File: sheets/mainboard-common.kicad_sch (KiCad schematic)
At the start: 46 parts, among them J1 Conn_01x04, J2 USB4105, J3 Conn_01x04, J4 Conn_01x16_Socket, J5 Conn_01x16_Socket, J6 Conn_01x16_Socket, J7 Conn_01x16_Socket, U2 AP22916, U3 AP22916

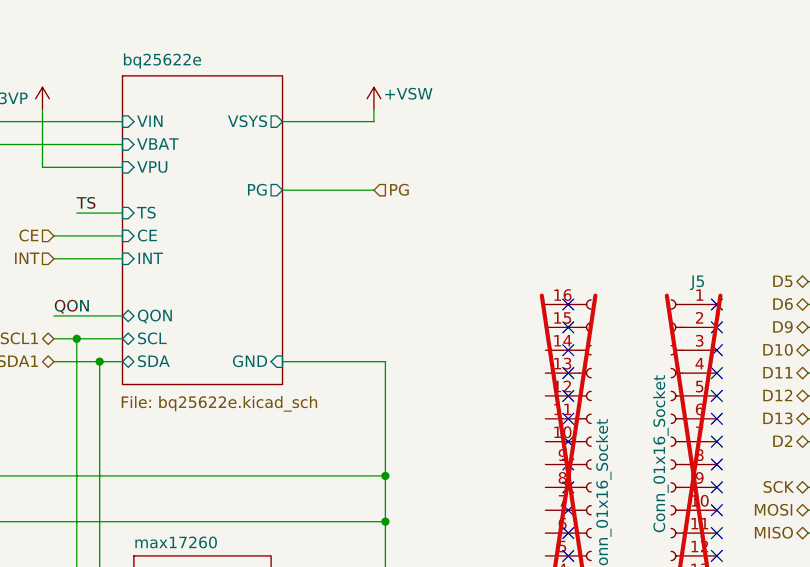
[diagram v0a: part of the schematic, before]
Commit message: Bring out ILIM
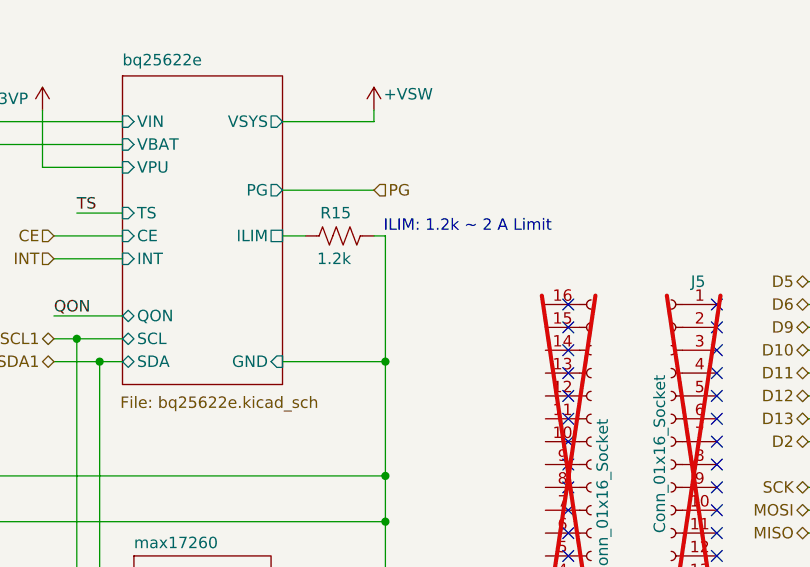
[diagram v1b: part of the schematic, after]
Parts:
- added R15: 1.2k, Resistor_SMD:R_0402_1005Metric, symbol Device:R_US
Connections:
- net GND: now also R15.2
- new net bq25622e/ILIM: R15.1
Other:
- sheet bq25622e ports: added ILIM; removed none
- note added: "ILIM: 1.2k ~ 2 A Limit"
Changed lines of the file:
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@@
 	)
 	(junction
+		(at 157.48 95.25)
+		(diameter 0)
+		(color 0 0 0 0)
+	)
+	(junction
 		(at 55.88 26.67)
 		(diameter 0)
@@
 	(wire
 		(pts
+			(xy 146.05 81.28) (xy 148.59 81.28)
+		)
+		(stroke
+			(width 0)
+			(type default)
+		)
+	)
+	(wire
+		(pts
 			(xy 146.05 30.48) (xy 146.05 33.02)
 		)
@@
 	(wire
 		(pts
+			(xy 157.48 81.28) (xy 157.48 95.25)
+		)
+		(stroke
+			(width 0)
+			(type default)
+		)
+	)
+	(wire
+		(pts
 			(xy 144.78 130.81) (xy 148.59 130.81)
 		)
@@
 	(wire
 		(pts
+			(xy 156.21 81.28) (xy 157.48 81.28)
+		)
+		(stroke
+			(width 0)
+			(type default)
+		)
+	)
+	(wire
+		(pts
 			(xy 247.65 35.56) (xy 245.11 35.56)
 		)
@@
 		)
 	)
+	(text "ILIM: 1.2k ~ 2 A Limit"
+		(exclude_from_sim no)
+		(at 166.624 80.264 0)
+		(effects
+			(font
+				(size 1.27 1.27)
+			)
+		)
+	)
 	(label "QON"
 		(at 242.57 96.52 180)
@@
 	)
 	(symbol
+		(lib_id "Device:R_US")
+		(at 152.4 81.28 90)
+		(unit 1)
+		(exclude_from_sim no)
+		(in_bom yes)
+		(on_board yes)
+		(dnp no)
+		(property "Reference" "R15"
+			(at 153.67 78.74 90)
+			(effects
+				(font
+					(size 1.27 1.27)
+				)
+				(justify left)
+			)
+		)
+		(property "Value" "1.2k"
+			(at 153.67 83.82 90)
+			(effects
+				(font
+					(size 1.27 1.27)
+				)
+				(justify left)
+			)
+		)
+		(property "Footprint" "Resistor_SMD:R_0402_1005Metric"
+			(at 152.654 80.264 90)
+			(effects
+				(font
+					(size 1.27 1.27)
+				)
+				(hide yes)
+			)
+		)
+		(property "Datasheet" ""
+			(at 152.4 81.28 0)
+			(effects
+				(font
+					(size 1.27 1.27)
+				)
+				(hide yes)
+			)
+		)
+		(property "Description" ""
+			(at 152.4 81.28 0)
+			(effects
+				(font
+					(size 1.27 1.27)
+				)
+				(hide yes)
+			)
+		)
+		(property "MPN" ""
+			(at 152.4 81.28 0)
+			(effects
+				(font
+					(size 1.27 1.27)
+				)
+				(hide yes)
+			)
+		)
+		(pin "1"
+		)
+		(pin "2"
+		)
+		(instances
+			(project "esp32s3-powerfeather"
+				(path "/5be6a852-fa78-49fa-bb8c-8d5ad39f4b26/a940761a-0d45-4491-ba89-ec093a8f239f"
+					(reference "R15")
+					(unit 1)
+				)
+			)
+		)
+	)
+	(symbol
 		(lib_id "Connector:TestPoint")
 		(at 71.12 171.45 270)
@@
 			)
 		)
+		(pin "ILIM" passive
+			(at 146.05 81.28 0)
+			(effects
+				(font
+					(size 1.27 1.27)
+				)
+				(justify right)
+			)
+		)

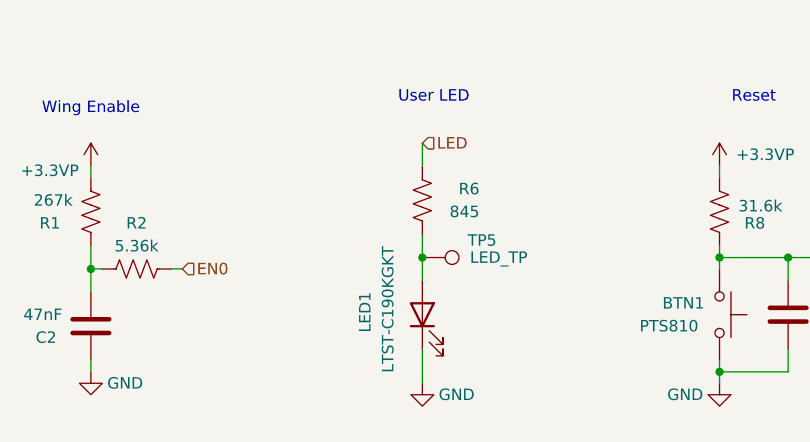
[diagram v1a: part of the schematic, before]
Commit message: Use same 1.2k for LED
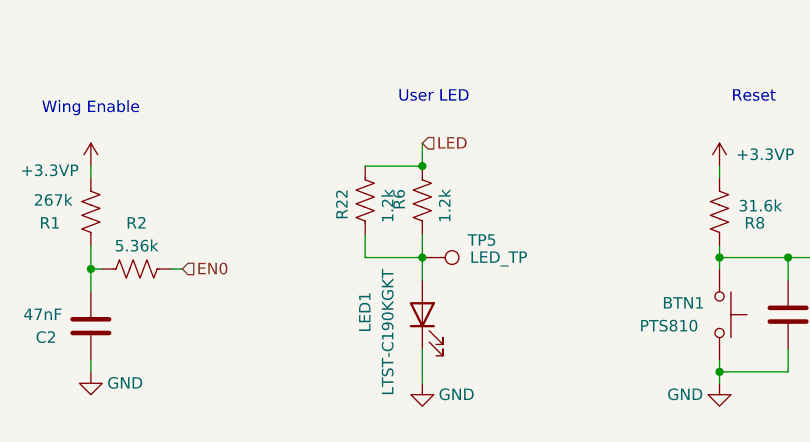
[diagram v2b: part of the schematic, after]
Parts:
- added R22: 1.2k, Resistor_SMD:R_0402_1005Metric, symbol Device:R_US
- R6: value 845 -> 1.2k; MPN 603-AC0402FR-07845RL -> (none)
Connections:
- net LED: now also R22.2
- net at LED1.2 (A), R6.1, TP5.1: now also R22.1
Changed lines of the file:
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@@
 	)
 	(junction
+		(at 71.12 161.29)
+		(diameter 0)
+		(color 0 0 0 0)
+	)
+	(junction
 		(at 143.51 171.45)
 		(diameter 0)
@@
 	(wire
 		(pts
+			(xy 64.77 161.29) (xy 71.12 161.29)
+		)
+		(stroke
+			(width 0)
+			(type default)
+		)
+	)
+	(wire
+		(pts
 			(xy 204.47 101.6) (xy 210.82 101.6)
 		)
@@
 	(wire
 		(pts
+			(xy 64.77 171.45) (xy 71.12 171.45)
+		)
+		(stroke
+			(width 0)
+			(type default)
+		)
+	)
+	(wire
+		(pts
 			(xy 33.02 102.87) (xy 33.02 107.95)
 		)
@@
 	(wire
 		(pts
+			(xy 64.77 168.91) (xy 64.77 171.45)
+		)
+		(stroke
+			(width 0)
+			(type default)
+		)
+	)
+	(wire
+		(pts
 			(xy 220.98 74.93) (xy 220.98 76.2)
 		)
@@
 		)
 		(property "Value" "LTST-C190KGKT"
-			(at 67.31 170.18 0)
+			(at 67.31 172.72 0)
 			(effects
 				(font
@@
 	(symbol
 		(lib_id "Device:R_US")
+		(at 71.12 165.1 180)
+		(unit 1)
+		(exclude_from_sim no)
+		(in_bom yes)
+		(on_board yes)
+		(dnp no)
+		(property "Reference" "R6"
+			(at 68.58 163.83 90)
+			(effects
+				(font
+					(size 1.27 1.27)
+				)
+				(justify left)
+			)
+		)
+		(property "Value" "1.2k"
+			(at 73.66 163.83 90)
+			(effects
+				(font
+					(size 1.27 1.27)
+				)
+				(justify left)
+			)
+		)
+		(property "Footprint" "Resistor_SMD:R_0402_1005Metric"
+			(at 70.104 164.846 90)
+			(effects
+				(font
+					(size 1.27 1.27)
+				)
+				(hide yes)
+			)
+		)
+		(property "Datasheet" ""
+			(at 71.12 165.1 0)
+			(effects
+				(font
+					(size 1.27 1.27)
+				)
+				(hide yes)
+			)
+		)
+		(property "Description" ""
+			(at 71.12 165.1 0)
+			(effects
+				(font
+					(size 1.27 1.27)
+				)
+				(hide yes)
+			)
+		)
+		(property "MPN" ""
+			(at 71.12 165.1 0)
+			(effects
+				(font
+					(size 1.27 1.27)
+				)
+				(hide yes)
+			)
+		)
+		(pin "1"
+		)
+		(pin "2"
+		)
+		(instances
+			(project "esp32s3-powerfeather"
+				(path "/5be6a852-fa78-49fa-bb8c-8d5ad39f4b26/a940761a-0d45-4491-ba89-ec093a8f239f"
+					(reference "R6")
+					(unit 1)
+				)
+			)
+		)
+	)
+	(symbol
+		(lib_id "Device:R_US")
 		(at 69.85 128.27 0)
 		(mirror y)
@@
 	(symbol
 		(lib_id "Device:R_US")
+		(at 64.77 165.1 180)
+		(unit 1)
+		(exclude_from_sim no)
+		(in_bom yes)
+		(on_board yes)
+		(dnp no)
+		(property "Reference" "R22"
+			(at 62.23 163.83 90)
+			(effects
+				(font
+					(size 1.27 1.27)
+				)
+				(justify left)
+			)
+		)
+		(property "Value" "1.2k"
+			(at 67.31 163.83 90)
+			(effects
+				(font
+					(size 1.27 1.27)
+				)
+				(justify left)
+			)
+		)
+		(property "Footprint" "Resistor_SMD:R_0402_1005Metric"
+			(at 63.754 164.846 90)
+			(effects
+				(font
+					(size 1.27 1.27)
+				)
+				(hide yes)
+			)
+		)
+		(property "Datasheet" ""
+			(at 64.77 165.1 0)
+			(effects
+				(font
+					(size 1.27 1.27)
+				)
+				(hide yes)
+			)
+		)
+		(property "Description" ""
+			(at 64.77 165.1 0)
+			(effects
+				(font
+					(size 1.27 1.27)
+				)
+				(hide yes)
+			)
+		)
+		(property "MPN" ""
+			(at 64.77 165.1 0)
+			(effects
+				(font
+					(size 1.27 1.27)
+				)
+				(hide yes)
+			)
+		)
+		(pin "1"
+		)
+		(pin "2"
+		)
+		(instances
+			(project "esp32s3-powerfeather"
+				(path "/5be6a852-fa78-49fa-bb8c-8d5ad39f4b26/a940761a-0d45-4491-ba89-ec093a8f239f"
+					(reference "R22")
+					(unit 1)
+				)
+			)
+		)
+	)
+	(symbol
+		(lib_id "Device:R_US")
 		(at 241.3 35.56 270)
 		(mirror x)
@@
 					(unit 1)
 				)
-			)
-		)
-	)
-	(symbol
-		(lib_id "Device:R_US")
-		(at 71.12 165.1 180)
-		(unit 1)
-		(exclude_from_sim no)
-		(in_bom yes)
-		(on_board yes)
-		(dnp no)
-		(property "Reference" "R6"
-			(at 77.47 163.83 0)
-			(effects
-				(font
-					(size 1.27 1.27)
-				)
-				(justify left)
-			)
-		)
-		(property "Value" "845"
-			(at 77.47 166.37 0)
-			(effects
-				(font
-					(size 1.27 1.27)
-				)
-				(justify left)
-			)
-		)
-		(property "Footprint" "Resistor_SMD:R_0402_1005Metric"
-			(at 70.104 164.846 90)
-			(effects
-				(font
-					(size 1.27 1.27)
-				)
-				(hide yes)
-			)
-		)
-		(property "Datasheet" "https://www.mouser.ph/datasheet/2/447/PYu_AC_51_RoHS_L_9-3005297.pdf"
-			(at 71.12 165.1 0)
-			(effects
-				(font
-					(size 1.27 1.27)
-				)
-				(hide yes)
-			)
-		)
-		(property "Description" ""
-			(at 71.12 165.1 0)
-			(effects
-				(font
-					(size 1.27 1.27)
-				)
-				(hide yes)
-			)
-		)
-		(property "MPN" "603-AC0402FR-07845RL"
-			(at 71.12 165.1 0)
-			(effects
-				(font
-					(size 1.27 1.27)
-				)
-				(hide yes)
-			)
-		)
-		(pin "1"
-		)
-		(pin "2"
-		)
-		(instances
-			(project "esp32s3-powerfeather"
-				(path "/5be6a852-fa78-49fa-bb8c-8d5ad39f4b26/a940761a-0d45-4491-ba89-ec093a8f239f"
-					(reference "R6")
-					(unit 1)
-				)

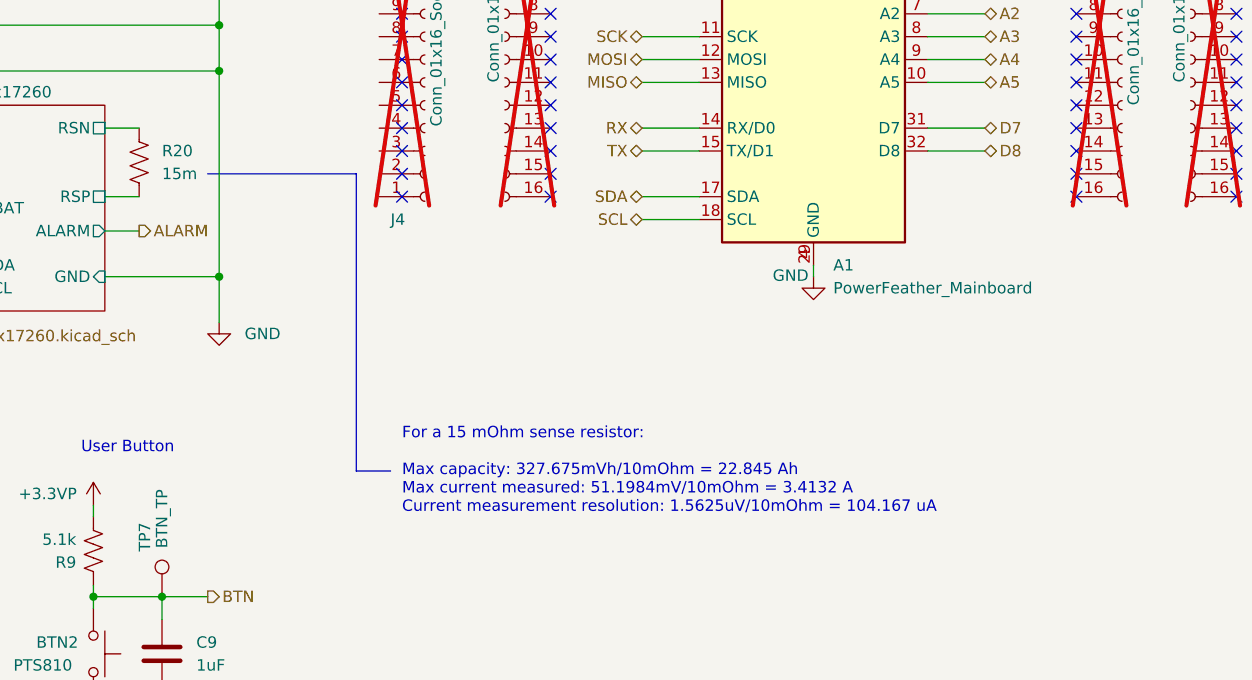
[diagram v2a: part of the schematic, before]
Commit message: Change sense resistor value
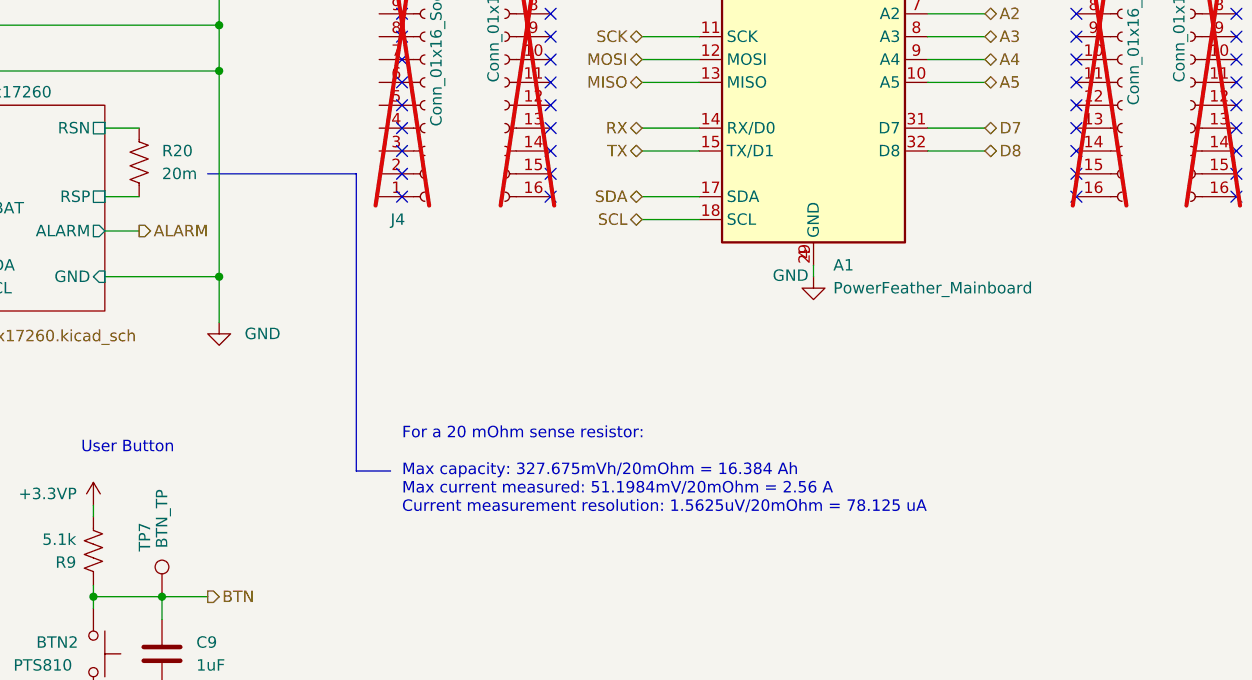
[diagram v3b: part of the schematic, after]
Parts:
- R20: value 15m -> 20m
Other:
- note added: "For a 20 mOhm sense resistor: Max capacity: 327.675mVh/20mOhm = 16.384 Ah Max current measured: 51.1984mV/20mOhm = 2.56 A Current measurement resolution: 1.5625uV/20mOhm = 78.125 uA"
- note removed: "For a 15 mOhm sense resistor: Max capacity: 327.675mVh/10mOhm = 22.845 Ah Max current measured: 51.1984mV/10mOhm = 3.4132 A Current measurement resolution: 1.5625uV/10mOhm = 104.167 uA"
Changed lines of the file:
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@@
 		)
 	)
-	(text "For a 15 mOhm sense resistor:\n\nMax capacity: 327.675mVh/10mOhm = 22.845 Ah\nMax current measured: 51.1984mV/10mOhm = 3.4132 A\nCurrent measurement resolution: 1.5625uV/10mOhm = 104.167 uA"
+	(text "For a 20 mOhm sense resistor:\n\nMax capacity: 327.675mVh/20mOhm = 16.384 Ah\nMax current measured: 51.1984mV/20mOhm = 2.56 A\nCurrent measurement resolution: 1.5625uV/20mOhm = 78.125 uA"
 		(exclude_from_sim no)
 		(at 177.8 157.48 0)
@@
 			)
 		)
-		(property "Value" "15m"
+		(property "Value" "20m"
 			(at 151.13 124.4599 0)
 			(effects

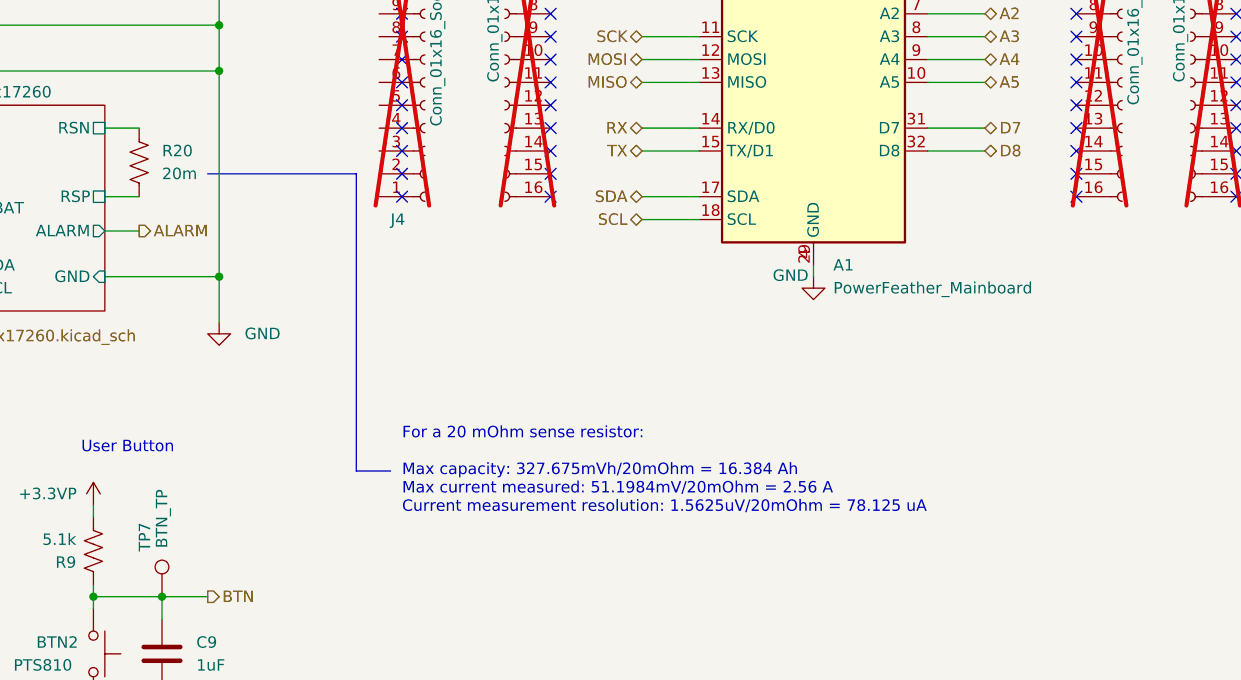
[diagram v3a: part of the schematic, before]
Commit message: Change rsense value
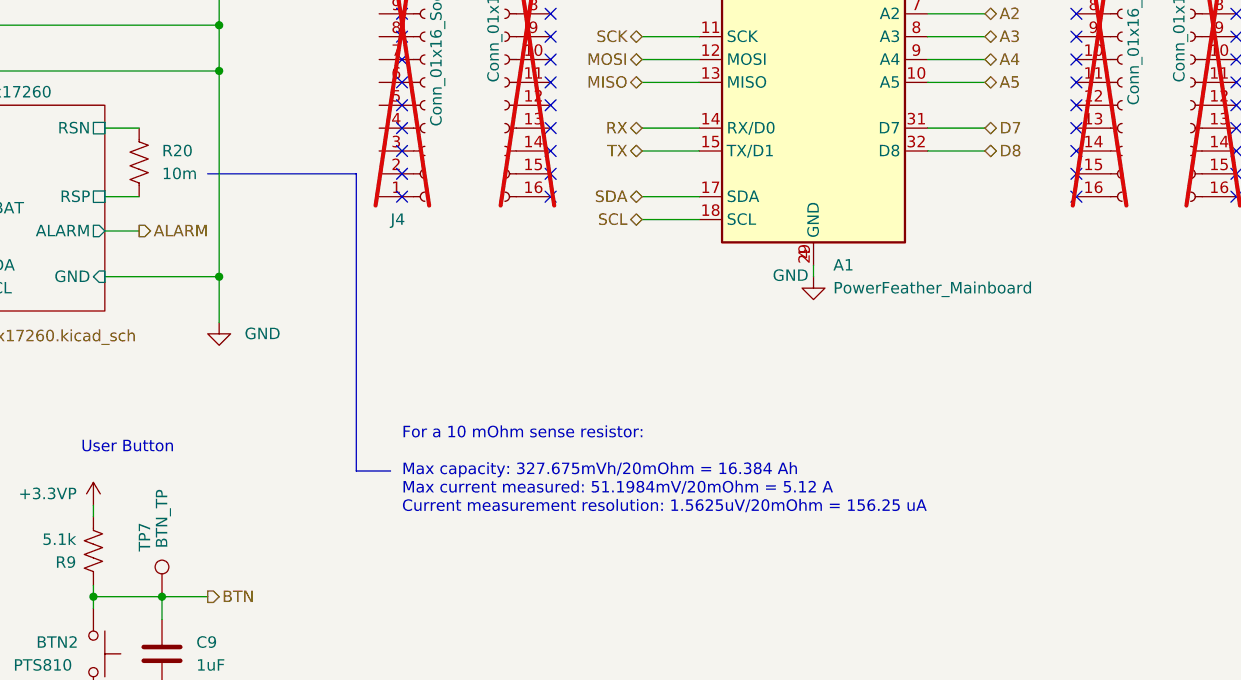
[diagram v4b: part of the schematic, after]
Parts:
- R20: value 20m -> 10m
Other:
- note added: "For a 10 mOhm sense resistor: Max capacity: 327.675mVh/20mOhm = 16.384 Ah Max current measured: 51.1984mV/20mOhm = 5.12 A Current measurement resolution: 1.5625uV/20mOhm = 156.25 uA"
- note removed: "For a 20 mOhm sense resistor: Max capacity: 327.675mVh/20mOhm = 16.384 Ah Max current measured: 51.1984mV/20mOhm = 2.56 A Current measurement resolution: 1.5625uV/20mOhm = 78.125 uA"
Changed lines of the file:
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@@
 		)
 	)
-	(text "For a 20 mOhm sense resistor:\n\nMax capacity: 327.675mVh/20mOhm = 16.384 Ah\nMax current measured: 51.1984mV/20mOhm = 2.56 A\nCurrent measurement resolution: 1.5625uV/20mOhm = 78.125 uA"
+	(text "For a 10 mOhm sense resistor:\n\nMax capacity: 327.675mVh/20mOhm = 16.384 Ah\nMax current measured: 51.1984mV/20mOhm = 5.12 A\nCurrent measurement resolution: 1.5625uV/20mOhm = 156.25 uA"
 		(exclude_from_sim no)
 		(at 177.8 157.48 0)
@@
 			)
 		)
-		(property "Value" "20m"
+		(property "Value" "10m"
 			(at 151.13 124.4599 0)
 			(effects
